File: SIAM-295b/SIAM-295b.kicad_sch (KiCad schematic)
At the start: 84 parts, among them J1 AudioJack2, J2 AudioJack2, SW1 SW_DPDT_x2, SW2 SW_Rotary_3x4, SW3 SW_Rotary_2x6, U1 TL074, U2 TL074, U3 TL074

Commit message: remove old files
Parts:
- added C34: 6n8, symbol Device:C
- added C35: 1n, symbol Device:C
- added C36, C37, C38, C39: C, symbol Device:C
- added R41: 18k, Resistor_THT:R_Axial_DIN0207_L6.3mm_D2.5mm_P10.16mm_Horizontal, symbol Device:R
- added R42: 27k, Resistor_THT:R_Axial_DIN0207_L6.3mm_D2.5mm_P10.16mm_Horizontal, symbol Device:R
- added R43, R44, R45, R46: 20k, Resistor_THT:R_Axial_DIN0207_L6.3mm_D2.5mm_P10.16mm_Horizontal, symbol Device:R
- C14: value 133n -> 47n; footprint Capacitor_THT:C_Rect_L10.0mm_W2.5mm_P7.50mm_MKS4 -> (none)
- C15: value 93n -> 1n5; footprint Capacitor_THT:C_Rect_L10.0mm_W2.5mm_P7.50mm_MKS4 -> (none)
- C16: value 62n -> 15n; footprint Capacitor_THT:C_Rect_L10.0mm_W2.5mm_P7.50mm_MKS4 -> (none)
- C17: value 41n -> 33n; footprint Capacitor_THT:C_Rect_L10.0mm_W2.5mm_P7.50mm_MKS4 -> (none)
- C18: value 27n -> 22n; footprint Capacitor_THT:C_Rect_L10.0mm_W2.5mm_P7.50mm_MKS4 -> (none)
- C19: value 17n -> 68n; footprint Capacitor_THT:C_Rect_L10.0mm_W2.5mm_P7.50mm_MKS4 -> (none)
- C20: value 3n9 -> 2n2; footprint Capacitor_THT:C_Rect_L10.0mm_W2.5mm_P7.50mm_MKS4 -> (none)
- C21: value 2n7 -> 100n; footprint Capacitor_THT:C_Rect_L10.0mm_W2.5mm_P7.50mm_MKS4 -> (none)
- C22: value 1n8 -> 33n; footprint Capacitor_THT:C_Rect_L10.0mm_W2.5mm_P7.50mm_MKS4 -> (none)
- C23: value 1n2 -> 3n3; footprint Capacitor_THT:C_Rect_L10.0mm_W2.5mm_P7.50mm_MKS4 -> (none)
- C24: value 770p -> C; footprint Capacitor_THT:C_Rect_L10.0mm_W2.5mm_P7.50mm_MKS4 -> (none)
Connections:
- net at C25.1, C25.2, R34.1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: now also C38.2, C39.2, R46.1; no longer C19.2, R40.1
- net at C24.1, C24.2, R33.1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: now also C36.2, C37.2, R45.1; no longer C18.2, R39.1
- net at R27.2, R28.1, SW3.5: now also C36.1, C37.1; no longer C18.1
- net at C16.2, R31.1, U3.3 (+): now also C14.2, C15.1, C15.2, R43.1; no longer C22.1, C22.2, R37.1
- net at C16.1, R25.2, R26.1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: now also C14.1
- net at C17.1, R26.2, R27.1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: now also C34.1
- net at R24.1, SW3.1: now also C21.1, C22.1; no longer C14.1
- net at R24.2, R25.1, SW3.2: now also C18.1, C19.1; no longer C15.1
- net at R28.2, SW3.6: now also C38.1, C39.1; no longer C19.1
- net at C17.2, R32.1, U3.5 (+): now also C34.2, C35.1, C35.2, R44.1; no longer C23.1, C23.2, R38.1
- new net: R38.1, R44.2
- new net: R39.1, R45.2
- new net: C21.2, C22.2, C23.1, C23.2, R29.1, R41.1, U2.10 (+)
- new net: C18.2, C19.2, C20.1, C20.2, R30.1, R42.1, U2.12 (+)
- new net: R37.1, R43.2
- new net: R35.1, R41.2
- new net: R36.1, R42.2
- new net: R40.1, R46.2
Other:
- moved on the sheet: R29, R30, R31, R32, R33, R34, U2C

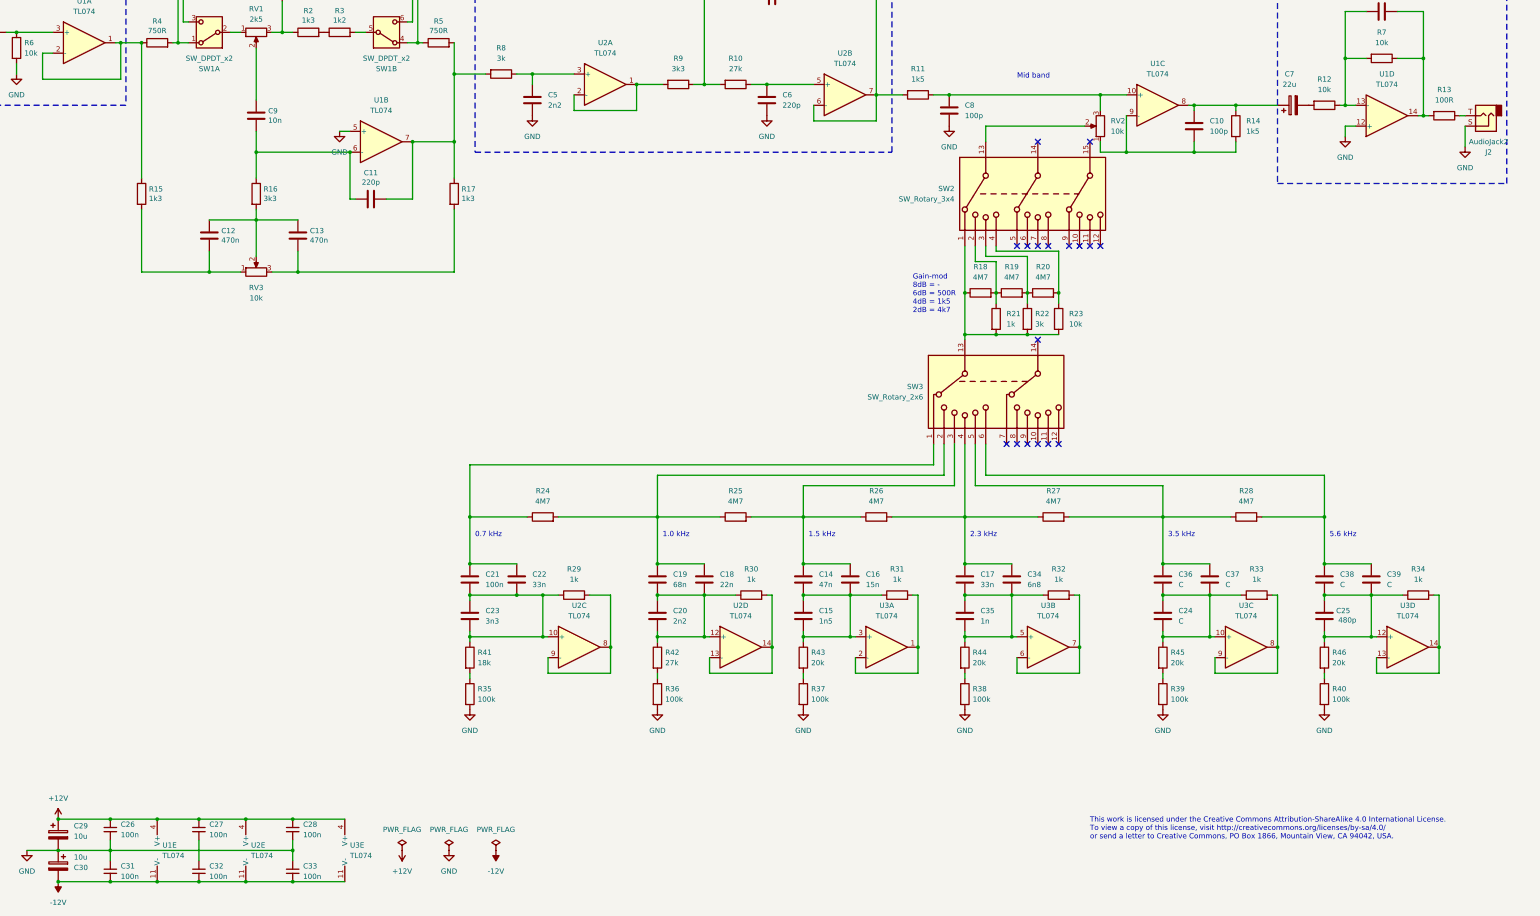
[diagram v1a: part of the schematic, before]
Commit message: update schematic
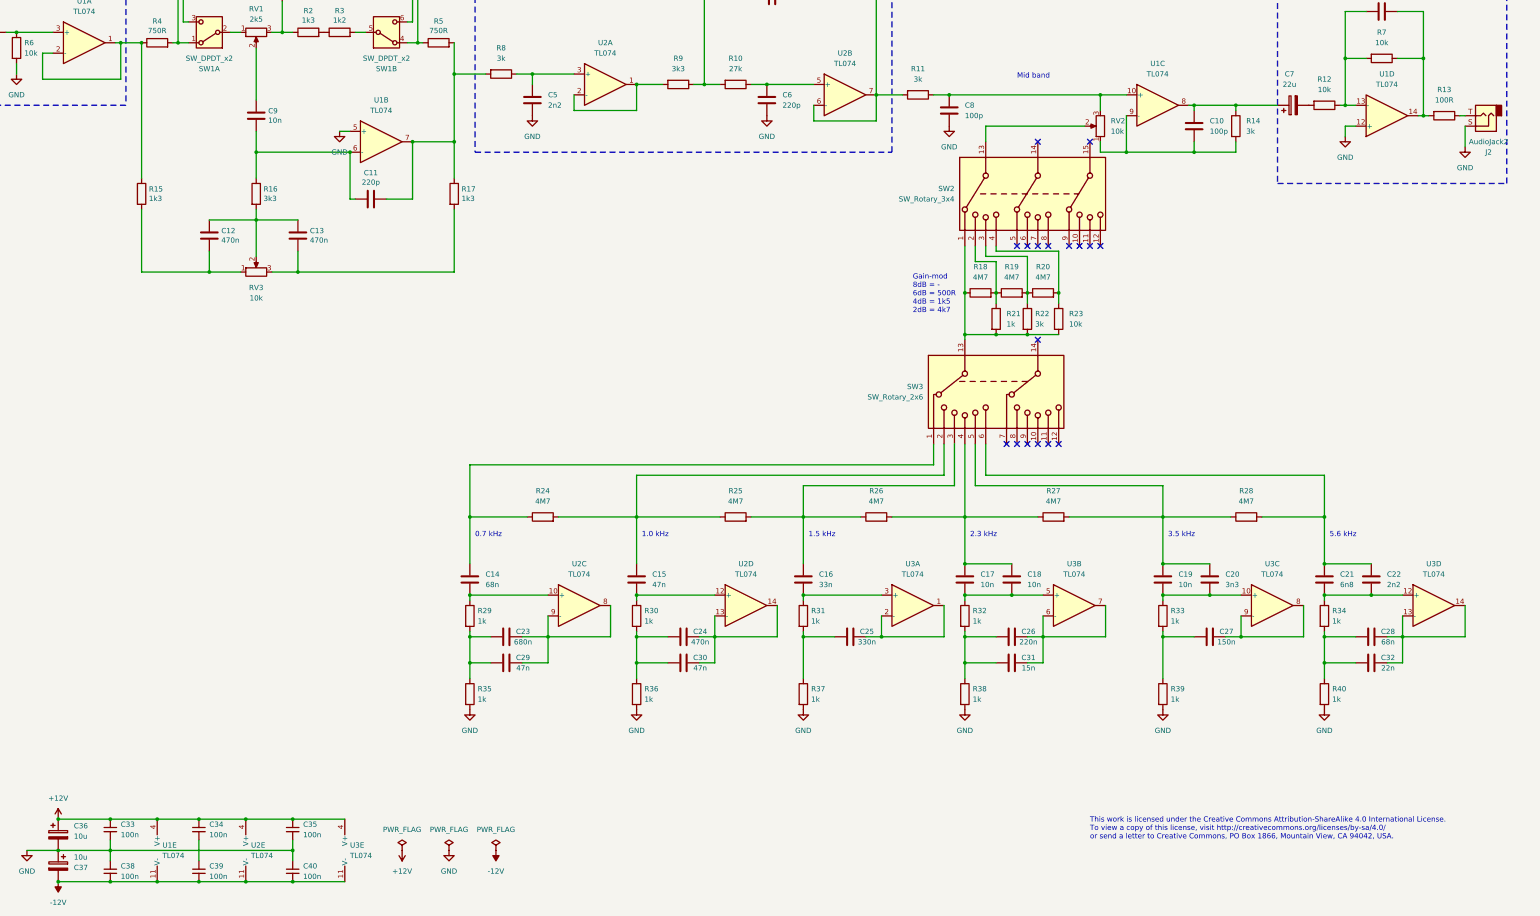
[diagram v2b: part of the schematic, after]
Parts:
- removed C14: 47n, symbol Device:C
- removed C34: 6n8, symbol Device:C
- removed C35: 1n, symbol Device:C
- removed C36, C37, C38, C39: C, symbol Device:C
- removed R41: 18k, Resistor_THT:R_Axial_DIN0207_L6.3mm_D2.5mm_P10.16mm_Horizontal, symbol Device:R
- removed R42: 27k, Resistor_THT:R_Axial_DIN0207_L6.3mm_D2.5mm_P10.16mm_Horizontal, symbol Device:R
- removed R43, R44, R45, R46: 20k, Resistor_THT:R_Axial_DIN0207_L6.3mm_D2.5mm_P10.16mm_Horizontal, symbol Device:R
- added C21: 6n8, symbol Device:C
- added C26: 220n, symbol Device:C
- added C27: 150n, symbol Device:C
- added C28: 68n, symbol Device:C
- added C29, C30: 47n, symbol Device:C
- added C31: 15n, symbol Device:C
- added C32: 22n, symbol Device:C
- C14: renamed from C21; value 100n -> 68n
- C15: value 1n5 -> 47n
- C16: value 15n -> 33n
- C17: value 33n -> 10n
- C18: value 22n -> 10n
- C19: value 68n -> 10n
- C20: value 2n2 -> 3n3
- C22: value 33n -> 2n2
- C23: value 3n3 -> 680n
- C24: value C -> 470n
- C25: value 480p -> 330n; footprint Capacitor_THT:C_Rect_L10.0mm_W2.5mm_P7.50mm_MKS4 -> (none)
- R11, R14: value 1k5 -> 3k
- R35, R36, R37, R38, R39, R40: value 100k -> 1k
- renumbered C26 to C33, C27 to C34, C28 to C35, C29 to C36, C30 to C37, C31 to C38, C32 to C39, C33 to C40
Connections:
- net at R34.1, U3.12 (+): now also C22.2, C21.2; no longer C25.1, C25.2
- net at U3.13 (-), U3.14: now also C28.2, C32.2; no longer R34.2
- net at C17.2, R32.1, U3.5 (+): now also C18.2
- net at R38.1: now also R32.2, C26.1, C31.1
- net at C16.2, R31.1, U3.3 (+): no longer C15.1, C15.2
- net at R39.1: now also R33.2, C27.1
- net at C14.1, R24.1, SW3.1: no longer C22.1
- net at C14.2, R29.1, U2.10 (+): no longer C22.2, C23.1, C23.2
- net at U3.1, U3.2 (-): now also C25.2; no longer R31.2
- net at R28.2, SW3.6: now also C22.1, C21.1
- net at U2.8, U2.9 (-): now also C23.2, C29.2; no longer R29.2
- net at R37.1: now also C25.1, R31.2
- net at R35.1: now also C23.1, R29.2, C29.1
- net at U2.13 (-), U2.14: now also C24.2, C30.2; no longer R30.2
- net at C17.1, R26.2, R27.1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: now also C18.1
- net at R24.2, R25.1, SW3.2: now also C15.1; no longer C18.1, C19.1
- net at R27.2, R28.1, SW3.5: now also C19.1, C20.1
- net at R33.1, U3.10 (+): now also C19.2, C20.2; no longer C24.1, C24.2
- net at U3.6 (-), U3.7: now also C26.2, C31.2; no longer R32.2
- net at R36.1: now also C24.1, R30.2, C30.1
- net at U3.8, U3.9 (-): now also C27.2; no longer R33.2
- net at R40.1: now also R34.2, C28.1, C32.1
- new net: C15.2, R30.1, U2.12 (+)
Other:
- moved on the sheet: C23, U2C
